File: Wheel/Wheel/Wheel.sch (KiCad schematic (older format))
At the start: 129 parts, among them J1 Conn_02x09_Odd_Even, J10 RJ45, J11 Screw_Terminal_01x02, J12 DS-201, J13 Conn_01x04, J14 Conn_02x13_Top_Bottom, J15 DB25_Female, J16 Conn_01x06, J17 Conn_01x07, J18 Conn_01x05, J19 RJ45, J2 RJ45, J20 DB9_Male, J21 DB9_Female, J3 RJ45, J4 RJ45, J5 USB_B, J6 Conn_02x09_Odd_Even, J7 Conn_02x10_Odd_Even, J8 RJ45, J9 RJ45, Q1 S8550, U1 MCP23S17_SP, U10 PC817, U11 PC817, U12 IP4220CZ6, U13 IP4220CZ6, U14 LTC2644, U15 PC817, U16 IP4220CZ6, U17 IP4220CZ6, U2 STM32F407VETx, U3 USBLC6-2SC6, U4 IP4220CZ6, U5 IP4220CZ6, U6 AMS1117, U7 4N35, U8 PC817, U9 PC817, Y1 32.768K, Y2 8MHz

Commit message: I've modified wheel's schematic and pcb
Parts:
- removed C3, C4: 6pF, Capacitor_SMD:C_0805_2012Metric, symbol Device:C
- removed JP1: SolderJumper_3_Bridged12, symbol Jumper:SolderJumper_3_Bridged12
- removed Q1: S8550, Package_TO_SOT_THT:TO-92_Inline, symbol Transistor_BJT:S8550
- removed R4: 10M, Resistor_SMD:R_0805_2012Metric, symbol Device:R
- removed R7: 1K5, Resistor_SMD:R_0805_2012Metric, symbol Device:R
- removed Y1: 32.768K, Crystal:Crystal_AT310_D3.0mm_L10.0mm_Horizontal_1EP_style2, symbol Device:Crystal_GND3
- D1, D10, D2, D3, D4, D5, D6, D7: value LED -> TO-2013BC-MRE; footprint (none) -> Diode_SMD:D_0805_2012Metric_Pad1.15x1.40mm_HandSolder
- D11: value LED -> TO-2013BC-PG; footprint (none) -> Diode_SMD:D_0805_2012Metric_Pad1.15x1.40mm_HandSolder
- D12: value LED -> TO-2013BC-BF; footprint (none) -> Diode_SMD:D_0805_2012Metric_Pad1.15x1.40mm_HandSolder
- D13: value LED -> TO-2013BC-MYF; footprint (none) -> Diode_SMD:D_0805_2012Metric_Pad1.15x1.40mm_HandSolder
- J1, J6: footprint (none) -> Connector_PinHeader_2.54mm:PinHeader_2x09_P2.54mm_Vertical
- J13: footprint (none) -> Connector_PinHeader_2.54mm:PinHeader_1x04_P2.54mm_Vertical
- J14: footprint Connector_IDC:IDC-Header_2x13-1MP_P2.54mm_Latch_Vertical -> Connector_IDC:IDC-Header_2x13_P2.54mm_Latch_Vertical
- J15: footprint (none) -> Connector_Dsub:DSUB-25_Female_Horizontal_P2.77x2.84mm_EdgePinOffset7.70mm_Housed_MountingHolesOffset9.12mm
- J16: footprint (none) -> Connector_PinHeader_2.54mm:PinHeader_1x06_P2.54mm_Vertical
- J17: footprint (none) -> Connector_PinHeader_2.54mm:PinHeader_1x07_P2.54mm_Vertical
- J18: footprint (none) -> Connector_PinHeader_2.54mm:PinHeader_1x05_P2.54mm_Vertical
- J20: footprint (none) -> Connector_Dsub:DSUB-9_Male_Horizontal_P2.77x2.84mm_EdgePinOffset7.70mm_Housed_MountingHolesOffset9.12mm
- J21: footprint (none) -> Connector_Dsub:DSUB-9_Female_Horizontal_P2.77x2.84mm_EdgePinOffset7.70mm_Housed_MountingHolesOffset9.12mm
- J5: footprint (none) -> Connector_USB:USB_B_Lumberg_2411_02_Horizontal
- JP2: footprint (none) -> Connector_PinSocket_2.54mm:PinSocket_1x03_P2.54mm_Vertical
- JP3: footprint (none) -> Connector_PinSocket_2.54mm:PinSocket_1x02_P2.54mm_Vertical
- JP4, JP5: footprint (none) -> Jumper:SolderJumper-3_P1.3mm_Bridged12_RoundedPad1.0x1.5mm
- JP6: footprint (none) -> Jumper:SolderJumper-2_P1.3mm_Open_RoundedPad1.0x1.5mm
- U14: footprint (none) -> Package_SO:MSOP-12_3x4mm_P0.65mm
- Y2: footprint Crystal:Crystal_HC49-U_Horizontal_1EP_style2 -> Crystal:Crystal_HC49-4H_Vertical
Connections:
- net labels added: OSC32_IN, OSC32_OUT
- net labels removed: DC12
- wire segments 516 -> 499
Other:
- moved on the sheet: R6

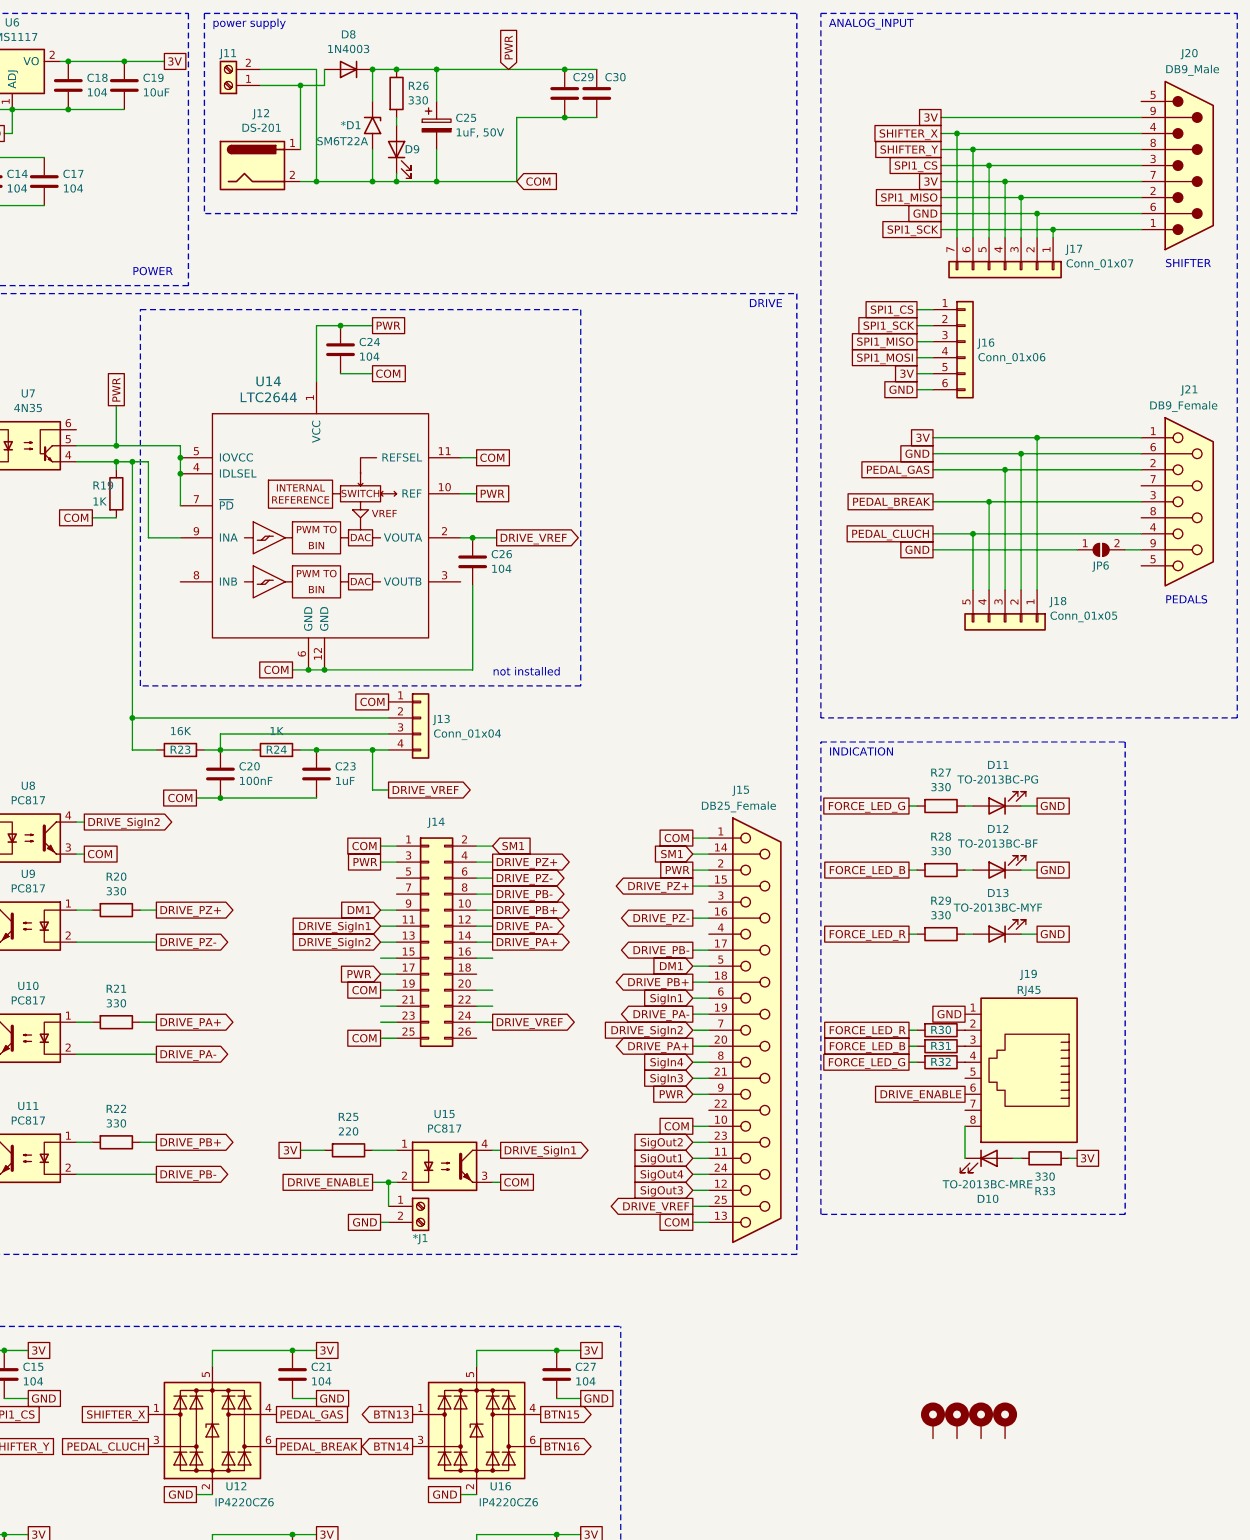
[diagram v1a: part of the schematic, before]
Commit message: I've modified wheel's PCB
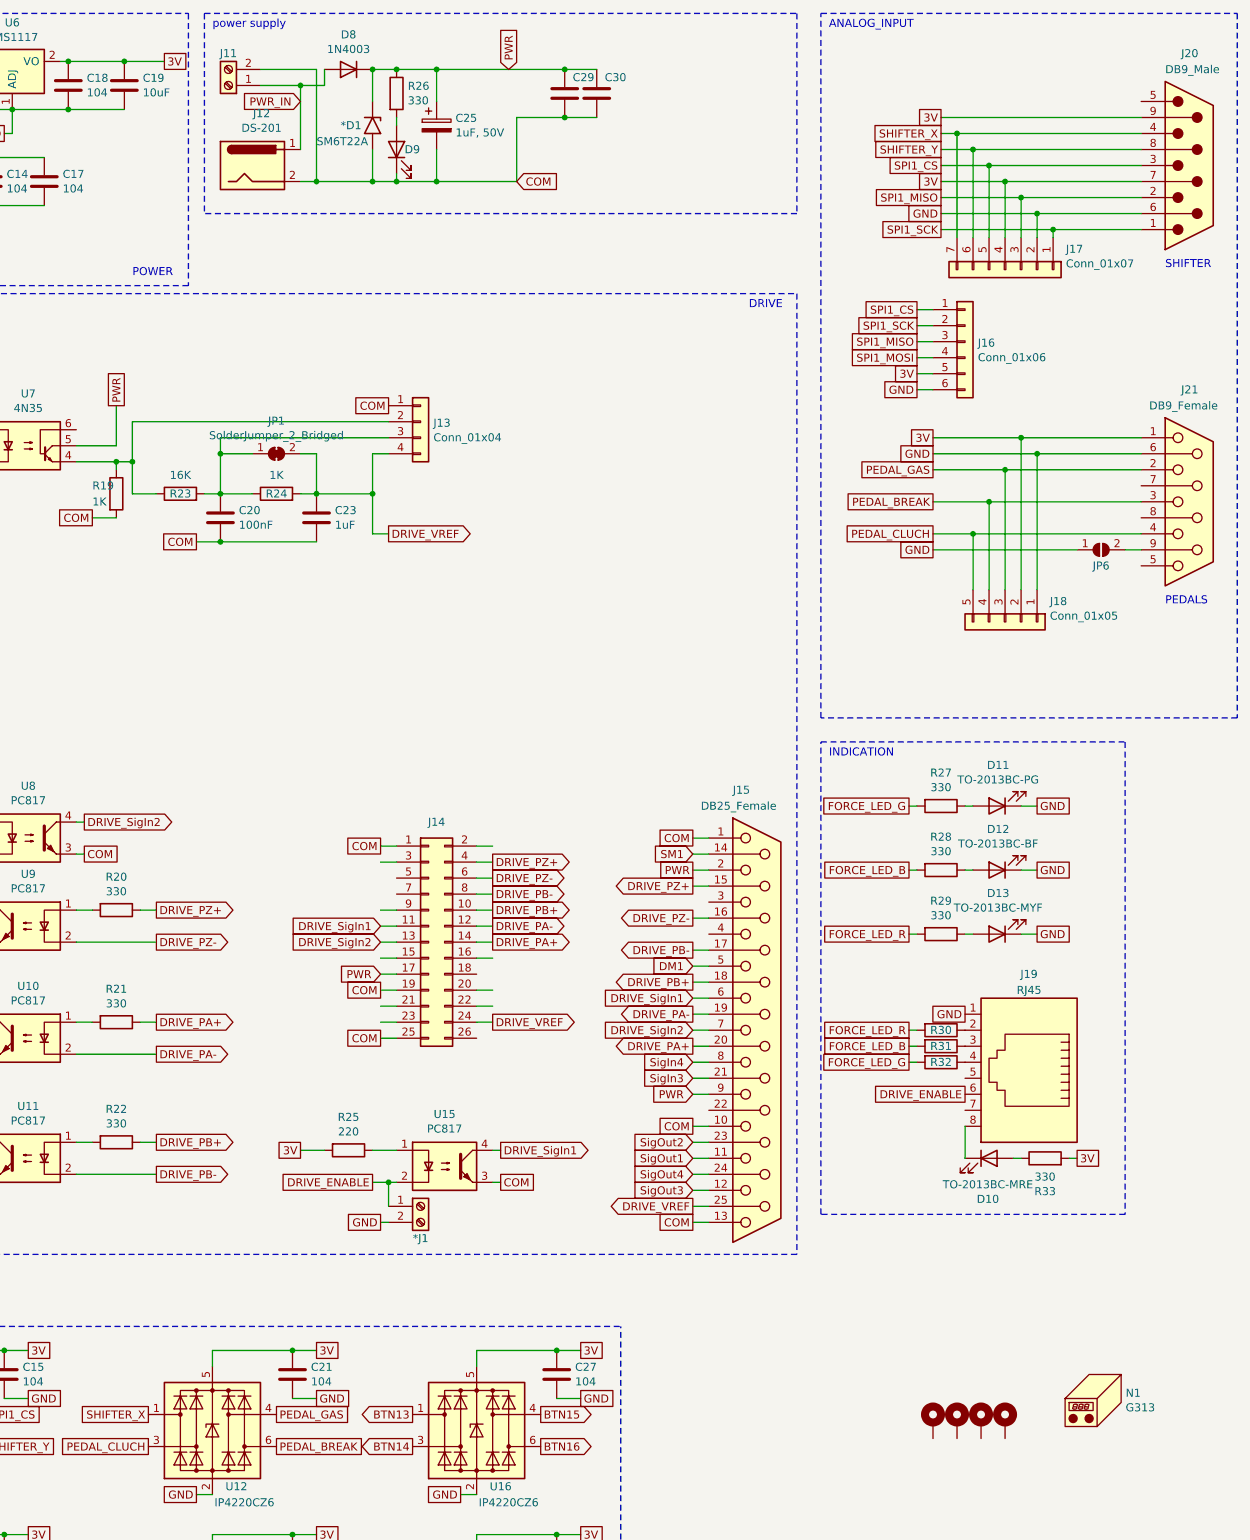
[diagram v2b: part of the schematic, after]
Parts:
- removed C24, C26: 104, Capacitor_SMD:C_0805_2012Metric, symbol Device:C
- removed U14: LTC2644, Package_SO:MSOP-12_3x4mm_P0.65mm, symbol KiCad-Lib:LTC2644
- added JP1: SolderJumper_2_Bridged, Jumper:SolderJumper-2_P1.3mm_Bridged_RoundedPad1.0x1.5mm, symbol Jumper:SolderJumper_2_Bridged
- added N1: G313, cases:CASE_G313, symbol Mechanical:Housing
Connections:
- net SigIn1 is gone; now on net DRIVE_SigIn1: J15.6
- net 3V: now also J18.2 (Pin_2); no longer J18.1 (Pin_1)
- net DM1: no longer J14.9 (Pin_9)
- net DRIVE_VREF: now also JP1.2 (B)
- net GND: now also J18.1 (Pin_1); no longer J18.2 (Pin_2)
- net PWR: no longer J14.3 (Pin_3)
- net SM1: no longer J14.2 (Pin_2)
- net PWR_IN: now reaches D8.2 (A), J11.1 (Pin_1), J12.1
- net at C20.1, J13.3 (Pin_3), R23.2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: now also JP1.1 (A)
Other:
- moved on the sheet: C20, C23, J13, R23, R24

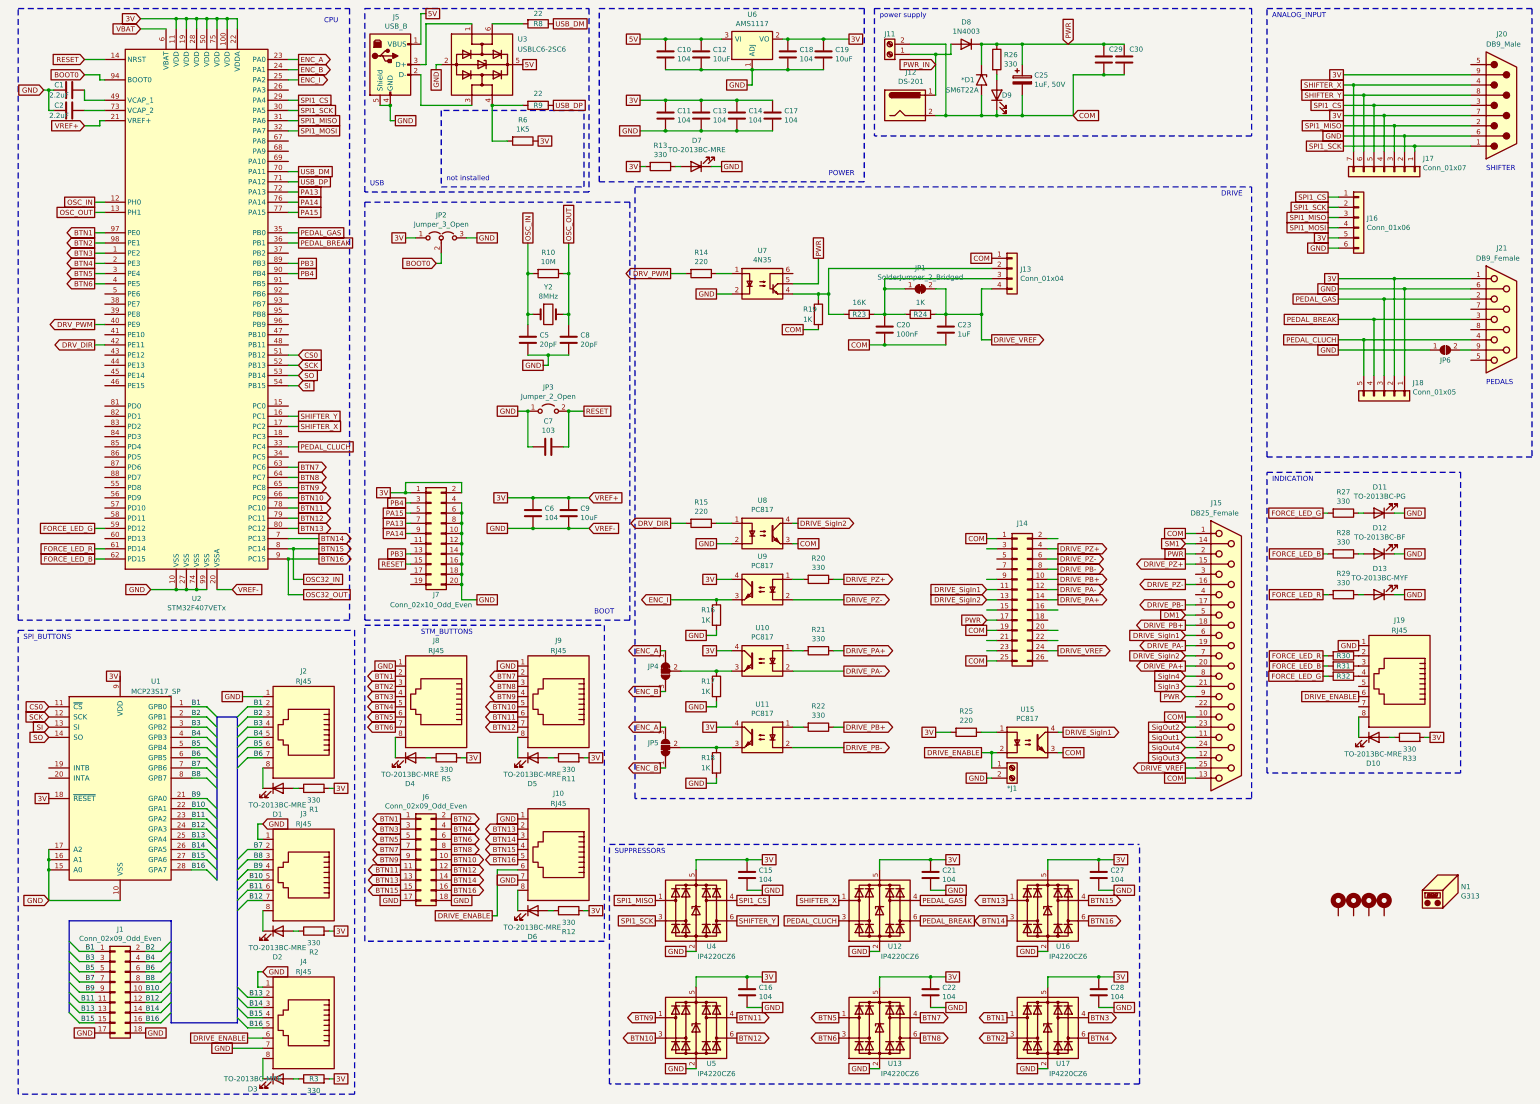
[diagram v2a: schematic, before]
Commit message: TDD Wheel's was changed
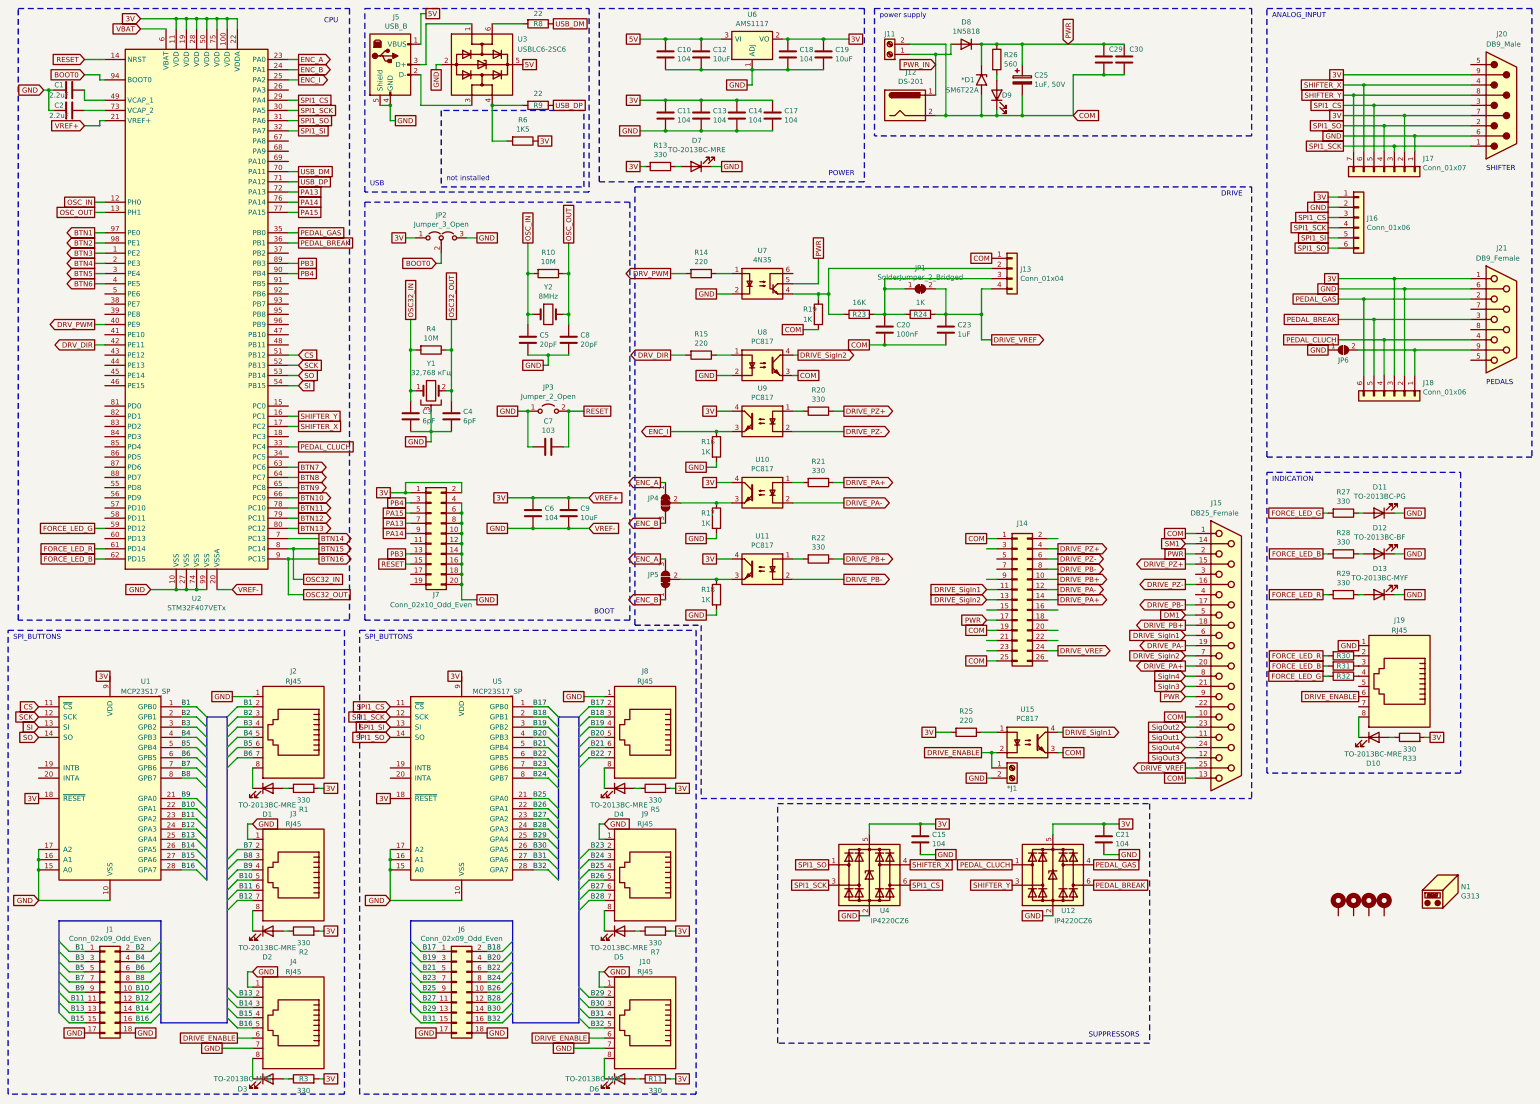
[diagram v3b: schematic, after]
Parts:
- removed C16, C22, C27, C28: 104, Capacitor_SMD:C_0805_2012Metric, symbol Device:C
- removed J18: Conn_01x05, Connector_PinHeader_2.54mm:PinHeader_1x05_P2.54mm_Vertical, symbol Connector_Generic:Conn_01x05
- removed R12: 330, Resistor_SMD:R_0805_2012Metric, symbol Device:R
- removed U13, U16, U17, U5: IP4220CZ6, Package_SO:TSOP-6_1.65x3.05mm_P0.95mm, symbol Power_Protection:USBLC6-4SC6
- added C3, C4: 6pF, Capacitor_SMD:C_0805_2012Metric, symbol Device:C
- added J18: Conn_01x06, Connector_PinHeader_2.54mm:PinHeader_1x06_P2.54mm_Vertical, symbol Connector_Generic:Conn_01x06
- added R4: 10M, Resistor_SMD:R_0805_2012Metric, symbol Device:R
- added R7: 330, Resistor_SMD:R_0805_2012Metric, symbol Device:R
- added U5: MCP23S17_SP, Package_DIP:DIP-28_W7.62mm, symbol Interface_Expansion:MCP23S17_SP
- added Y1: 32,768 кГц, Crystal:Crystal_C26-LF_D2.1mm_L6.5mm_Horizontal_1EP_style2, symbol Device:Crystal_GND3
- D8: value 1N4003 -> 1N5818
- J1, J6: footprint Connector_PinHeader_2.54mm:PinHeader_2x09_P2.54mm_Vertical -> Connector_PinHeader_2.54mm:PinHeader_1x18_P2.54mm_Vertical
- R26: value 330 -> 560
- U10, U11, U15, U8, U9: footprint Package_DIP:DIP-4_W7.62mm -> Package_DIP:SMDIP-4_W7.62mm
- U7: footprint Package_DIP:DIP-6_W7.62mm -> Package_DIP:SMDIP-6_W7.62mm
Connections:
- net 3V: now also J16.1 (Pin_1), J17.2 (Pin_2), J18.3 (Pin_3), R7.2, U5.18 (~RESET~), U5.9 (VDD); no longer J16.5 (Pin_5), J17.4 (Pin_4)
- net BTN1: no longer J6.1 (Pin_1), J8.2
- net BTN10: no longer J6.10 (Pin_10), J9.5
- net BTN11: no longer J6.11 (Pin_11), J9.6
- net BTN12: no longer J6.12 (Pin_12), J9.7
- net BTN13: no longer J10.2, J6.13 (Pin_13)
- net BTN14: no longer J10.3, J6.14 (Pin_14)
- net BTN15: now also C3.1, R4.2, Y1.1; no longer J10.4, J6.15 (Pin_15)
- net BTN16: now also C4.1, R4.1, Y1.2; no longer J10.5, J6.16 (Pin_16)
- net BTN2: no longer J6.2 (Pin_2), J8.3
- net BTN3: no longer J6.3 (Pin_3), J8.4
- net BTN4: no longer J6.4 (Pin_4), J8.5
- net BTN5: no longer J6.5 (Pin_5), J8.6
- net BTN6: no longer J6.6 (Pin_6), J8.7
- net BTN7: no longer J6.7 (Pin_7), J9.2
- net BTN8: no longer J6.8 (Pin_8), J9.3
- net BTN9: no longer J6.9 (Pin_9), J9.4
- net GND: now also J16.2 (Pin_2), J17.1 (Pin_1), C3.2, C4.2, J18.2 (Pin_2), U5.10 (VSS), U5.15 (A0), U5.16 (A1), U5.17 (A2), Y1.3; no longer J16.6 (Pin_6), J17.2 (Pin_2)
- net PEDAL_BREAK: now also J18.5 (Pin_5)
- net PEDAL_CLUCH: now also U12.1 (I/O1), J18.4 (Pin_4); no longer U12.3 (I/O2)
- net PEDAL_GAS: now also J18.6 (Pin_6)
- net SHIFTER_X: now also J17.6 (Pin_6), U4.4 (I/O3); no longer J17.7 (Pin_7), U12.1 (I/O1)
- net SHIFTER_Y: now also J17.7 (Pin_7), U12.3 (I/O2); no longer J17.6 (Pin_6), U4.6 (I/O4)
- net SPI1_CS: now also J16.3 (Pin_3), U4.6 (I/O4), U5.11 (~CS~); no longer J16.1 (Pin_1), U4.4 (I/O3)
- net SPI1_SCK: now also J16.4 (Pin_4), J17.3 (Pin_3), U5.12 (SCK); no longer J16.2 (Pin_2), J17.1 (Pin_1)
- net at D5.2 (A): now also R7.1; no longer R11.1
- net at D6.2 (A): now also R11.1
- net at J21.9, JP6.2 (B): now also J18.1 (Pin_1)
- net CS0 renamed CS
- net SPI1_MISO renamed SPI1_SO
- net SPI1_SO: now also J16.6 (Pin_6), J17.4 (Pin_4), U5.14 (SO); no longer J16.3 (Pin_3), J17.3 (Pin_3)
- net SPI1_MOSI renamed SPI1_SI
- net SPI1_SI: now also J16.5 (Pin_5), U5.13 (SI); no longer J16.4 (Pin_4)
- new net B17: J6.1 (Pin_1), J8.2, U5.1 (GPB0)
- new net B18: J6.2 (Pin_2), J8.3, U5.2 (GPB1)
- new net B19: J6.3 (Pin_3), J8.4, U5.3 (GPB2)
- new net B20: J6.4 (Pin_4), J8.5, U5.4 (GPB3)
- new net B21: J6.5 (Pin_5), J8.6, U5.5 (GPB4)
- new net B22: J6.6 (Pin_6), J8.7, U5.6 (GPB5)
- new net B23: J6.7 (Pin_7), J9.2, U5.7 (GPB6)
- new net B24: J6.8 (Pin_8), J9.3, U5.8 (GPB7)
- new net B25: J6.9 (Pin_9), J9.4, U5.21 (GPA0)
- new net B26: J6.10 (Pin_10), J9.5, U5.22 (GPA1)
- new net B27: J6.11 (Pin_11), J9.6, U5.23 (GPA2)
- new net B28: J6.12 (Pin_12), J9.7, U5.24 (GPA3)
- new net B29: J10.2, J6.13 (Pin_13), U5.25 (GPA4)
- new net B30: J10.3, J6.14 (Pin_14), U5.26 (GPA5)
- new net B31: J10.4, J6.15 (Pin_15), U5.27 (GPA6)
- new net B32: J10.5, J6.16 (Pin_16), U5.28 (GPA7)
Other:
- note removed: "STM_BUTTONS"
- moved on the sheet: C15, C21, D1, D2, D3, J1, J2, J3, J4, JP4, JP5, JP6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
